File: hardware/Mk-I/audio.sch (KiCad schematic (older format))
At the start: 10 parts, among them U1 AP7313-18-SR-G-7, U5 SGTL5000

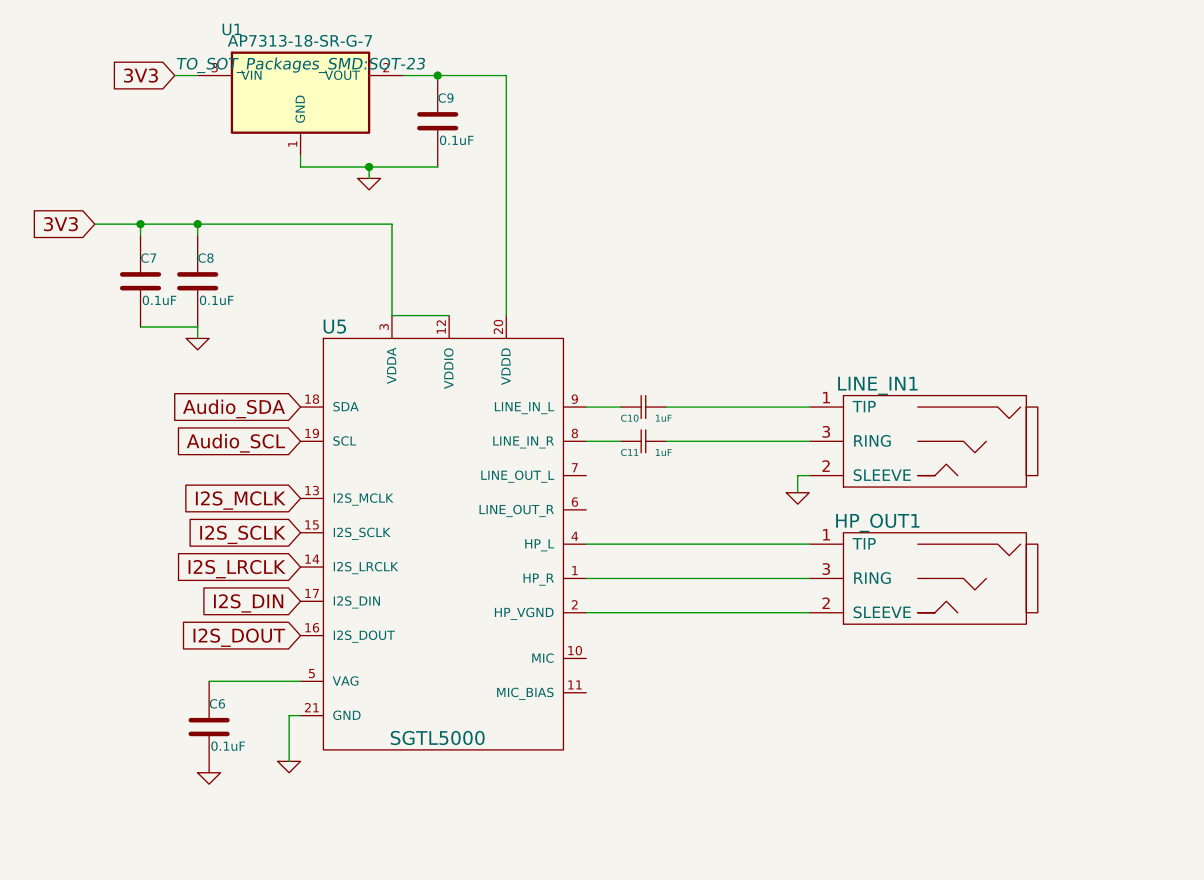
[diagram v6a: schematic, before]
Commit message: HW: Update parts value
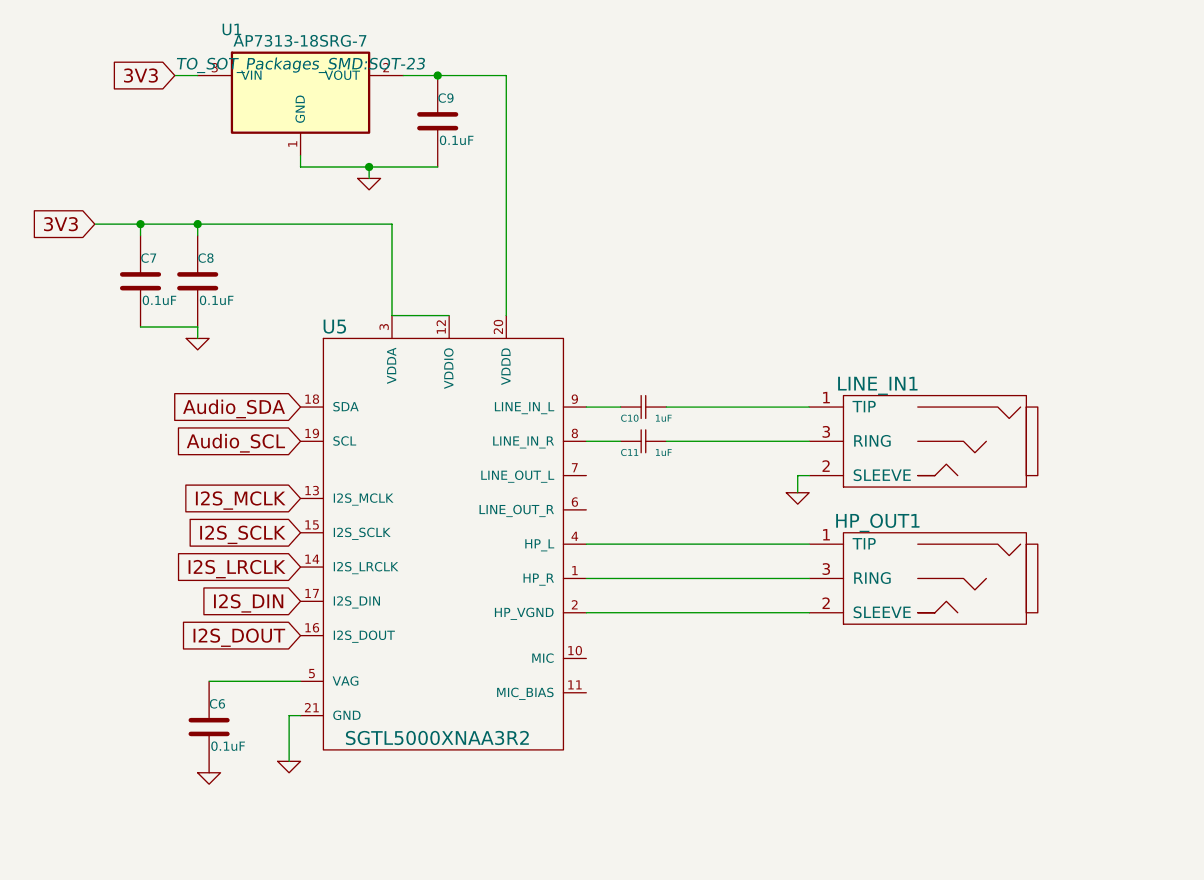
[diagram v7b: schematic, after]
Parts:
- HP_OUT1, LINE_IN1: value 3.5_audio_jack -> 1503 02
- U1: value AP7313-18-SR-G-7 -> AP7313-18SRG-7
- U5: value SGTL5000 -> SGTL5000XNAA3R2
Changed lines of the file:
@@
 P 4750 3200
 F 0 "U5" H 4650 3450 60  0000 C CNN
-F 1 "SGTL5000" H 5100 1650 60  0000 C CNN
+F 1 "SGTL5000XNAA3R2" H 5100 1650 60  0000 C CNN
 F 2 "Housings_DFN_QFN:UQFN-20-1EP_3x3mm_Pitch0.4mm" H 4750 3150 60  0001 C CNN
 F 3 "" H 4750 3150 60  0001 C CNN
@@
 P 7100 4425
 F 0 "HP_OUT1" H 7175 3800 60  0000 C CNN
-F 1 "3.5_audio_jack" H 7100 4425 60  0001 C CNN
+F 1 "1503 02" H 7100 4425 60  0001 C CNN
 F 2 "POSS:lumberg_3.5_audio_jack_1503_02" H 7100 4425 60  0001 C CNN
 F 3 "" H 7100 4425 60  0001 C CNN
@@
 P 7100 3825
 F 0 "LINE_IN1" H 7175 3200 60  0000 C CNN
-F 1 "3.5_audio_jack" H 6950 3200 60  0001 C CNN
+F 1 "1503 02" H 6950 3200 60  0001 C CNN
 F 2 "POSS:lumberg_3.5_audio_jack_1503_02" H 7100 3825 60  0001 C CNN
 F 3 "" H 7100 3825 60  0001 C CNN
@@
 P 4500 1900
 F 0 "U1" H 4200 2150 50  0000 C CNN
-F 1 "AP7313-18-SR-G-7" H 4500 2100 50  0000 C CNN
+F 1 "AP7313-18SRG-7" H 4500 2100 50  0000 C CNN
 F 2 "TO_SOT_Packages_SMD:SOT-23" H 4500 2000 50  0000 C CIN
 F 3 "" H 4500 1900 50  0000 C CNN
